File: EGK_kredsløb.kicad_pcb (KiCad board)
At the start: 2 copper layers, 103 x 72 mm, 25 parts, among them U1 INA114AP, U2 MCP6004, U3 MCP6004

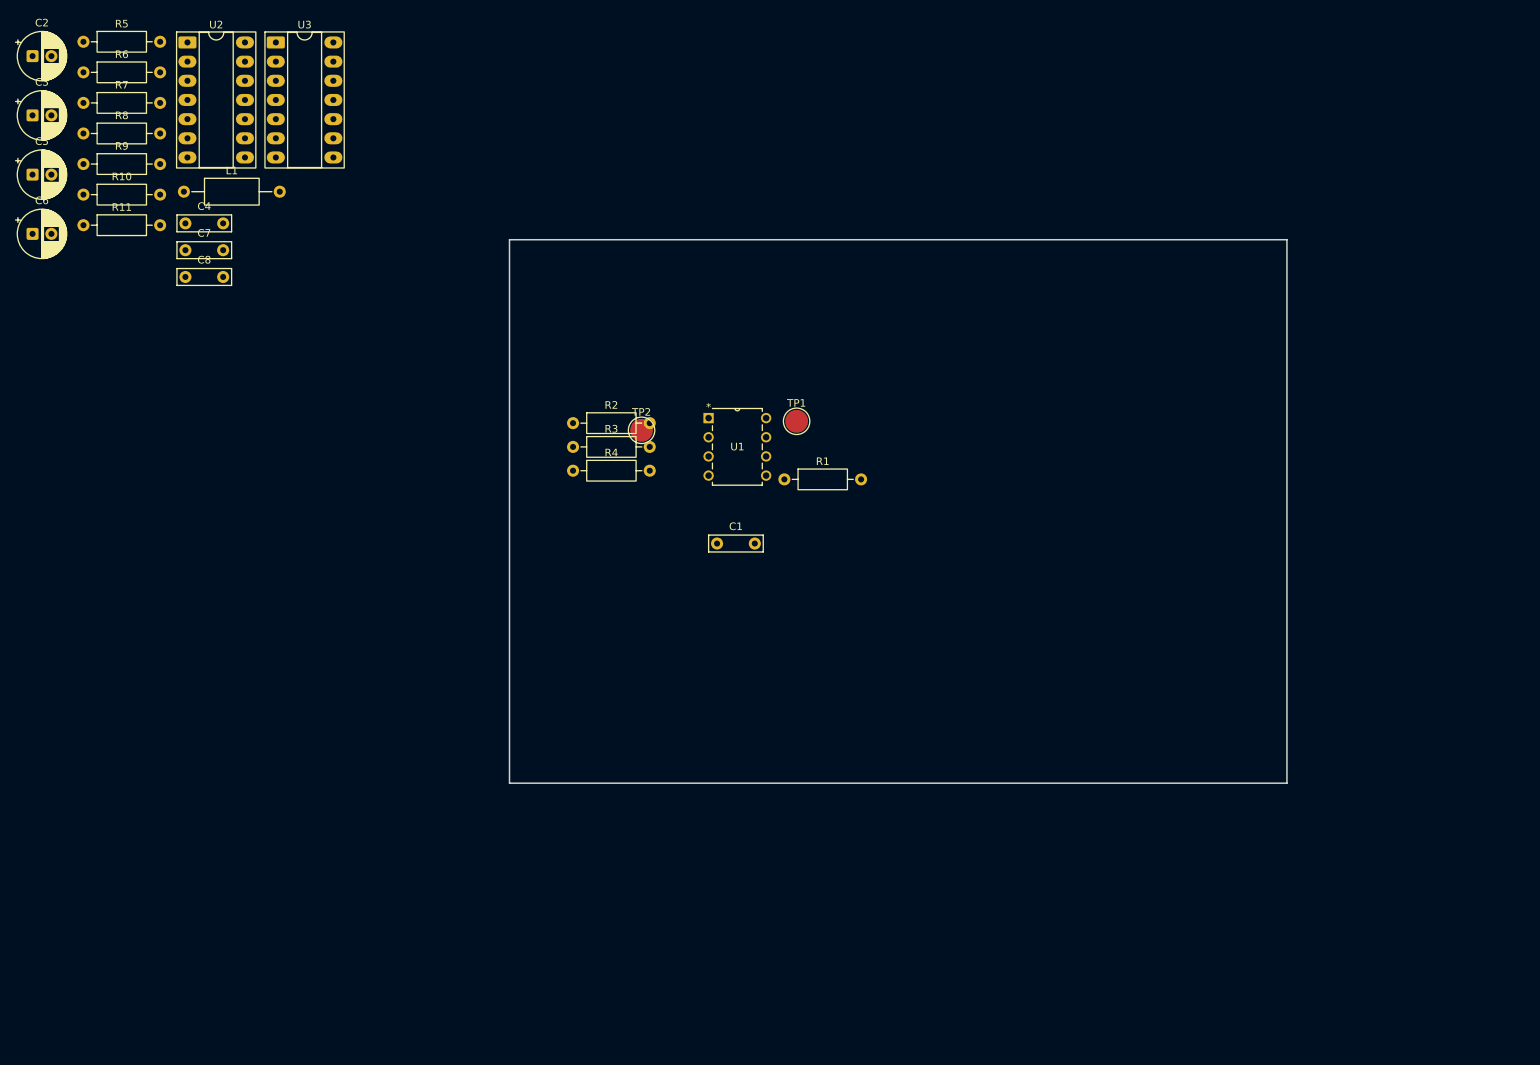
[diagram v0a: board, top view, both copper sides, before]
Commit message: finished schematic, missing AUX
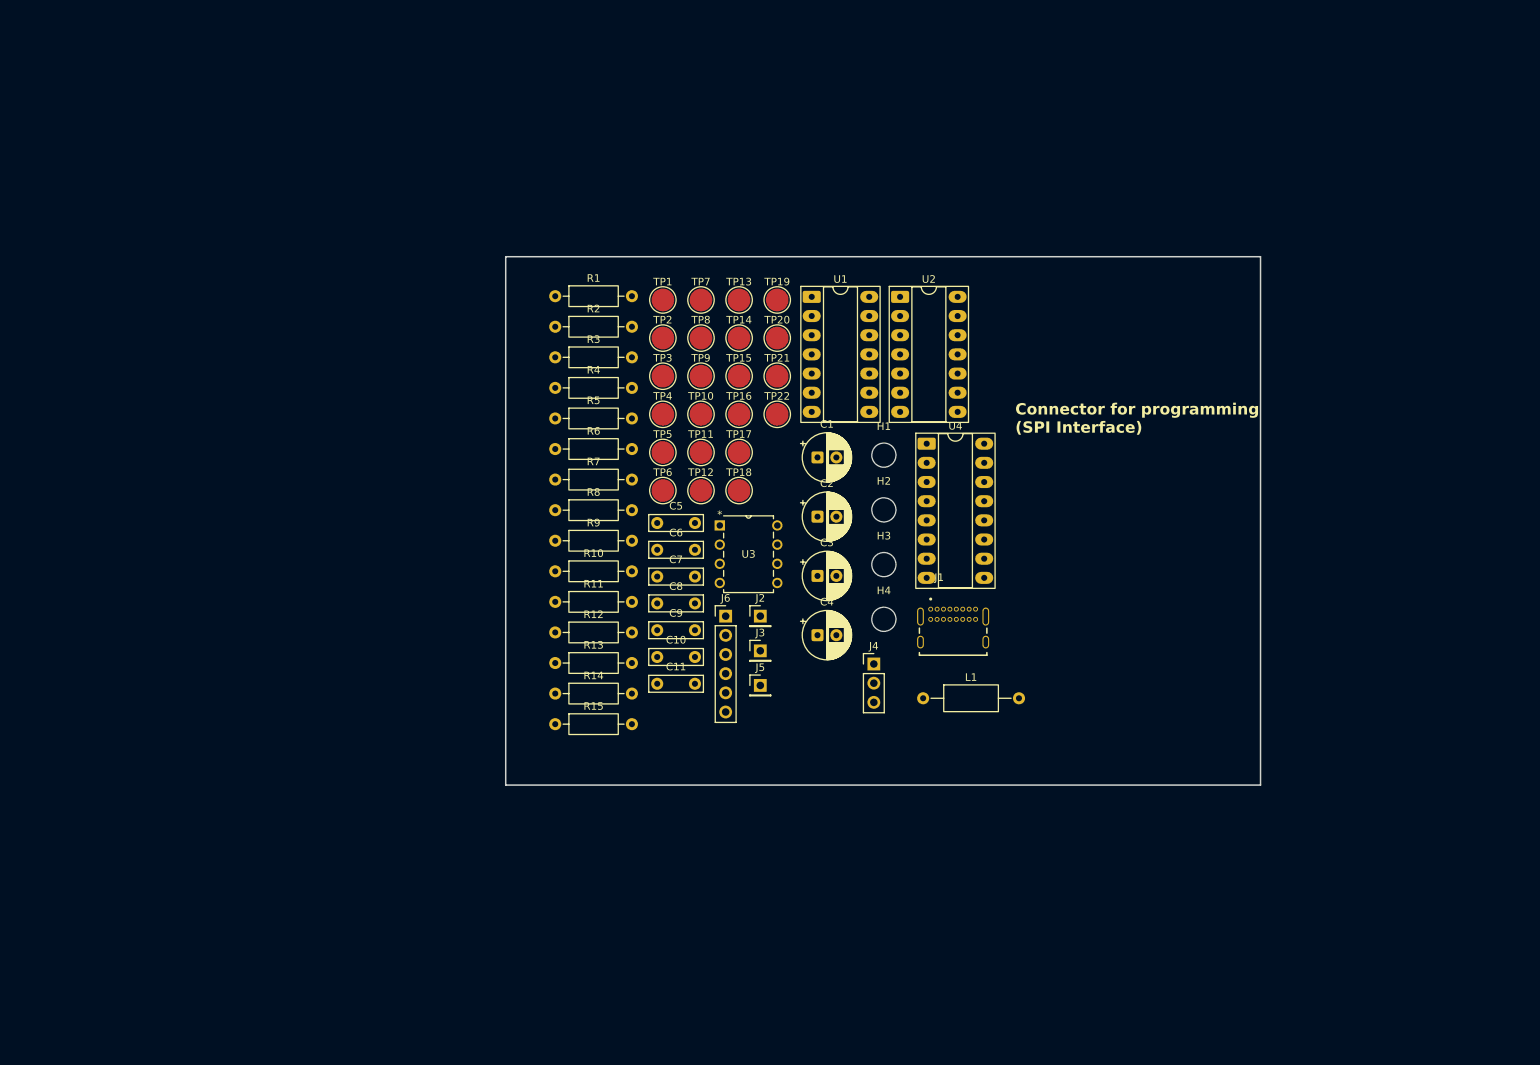
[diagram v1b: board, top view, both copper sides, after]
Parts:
- added C10: 100n, Capacitor_THT:C_Rect_L7.0mm_W2.0mm_P5.00mm, F.Cu at (85.1, 83.0)
- added C11: 10n, Capacitor_THT:C_Rect_L7.0mm_W2.0mm_P5.00mm, F.Cu at (85.1, 86.6)
- added C9: 100n, Capacitor_THT:C_Rect_L7.0mm_W2.0mm_P5.00mm, F.Cu at (85.1, 79.5)
- added H1: MountingHole, MountingHole:MountingHole_3.2mm_M3_ISO7380, F.Cu at (115.1, 56.3)
- added H2: MountingHole, MountingHole:MountingHole_3.2mm_M3_ISO7380, F.Cu at (115.1, 63.5)
- added H3: MountingHole, MountingHole:MountingHole_3.2mm_M3_ISO7380, F.Cu at (115.1, 70.8)
- added H4: MountingHole, MountingHole:MountingHole_3.2mm_M3_ISO7380, F.Cu at (115.1, 78.0)
- added J1: USB4085-GF-A_REVB, connector:GCT_USB4085-GF-A_REVB, F.Cu at (124.3, 81.1)
- added J2: Conn_01x01_Pin, Connector_PinHeader_2.54mm:PinHeader_1x01_P2.54mm_Vertical, F.Cu at (98.7, 77.6)
- added J3: Conn_01x01_Pin, Connector_PinHeader_2.54mm:PinHeader_1x01_P2.54mm_Vertical, F.Cu at (98.7, 82.2)
- added J4: Conn_01x03, Connector_PinHeader_2.54mm:PinHeader_1x03_P2.54mm_Vertical, F.Cu at (113.8, 84.0)
- added J5: Conn_01x01_Pin, Connector_PinHeader_2.54mm:PinHeader_1x01_P2.54mm_Vertical, F.Cu at (98.7, 86.8)
- added J6: Conn_01x06_Pin, Connector_PinHeader_2.54mm:PinHeader_1x06_P2.54mm_Vertical, F.Cu at (94.1, 77.6)
- added R12: 390k, Resistor_THT:R_Axial_DIN0207_L6.3mm_D2.5mm_P10.16mm_Horizontal, F.Cu at (71.6, 79.8)
- added R13: 390k, Resistor_THT:R_Axial_DIN0207_L6.3mm_D2.5mm_P10.16mm_Horizontal, F.Cu at (71.6, 83.8)
- added R14: 10k, Resistor_THT:R_Axial_DIN0207_L6.3mm_D2.5mm_P10.16mm_Horizontal, F.Cu at (71.6, 87.9)
- added R15: 10k, Resistor_THT:R_Axial_DIN0207_L6.3mm_D2.5mm_P10.16mm_Horizontal, F.Cu at (71.6, 91.9)
- added TP10: TestPoint, TestPoint:TestPoint_Pad_D3.0mm, F.Cu at (90.9, 50.9)
- added TP11: TestPoint, TestPoint:TestPoint_Pad_D3.0mm, F.Cu at (90.9, 55.9)
- added TP12: TestPoint, TestPoint:TestPoint_Pad_D3.0mm, F.Cu at (90.9, 61.0)
- added TP13: TestPoint, TestPoint:TestPoint_Pad_D3.0mm, F.Cu at (95.9, 35.7)
- added TP14: TestPoint, TestPoint:TestPoint_Pad_D3.0mm, F.Cu at (95.9, 40.8)
- added TP15: TestPoint, TestPoint:TestPoint_Pad_D3.0mm, F.Cu at (95.9, 45.8)
- added TP16: TestPoint, TestPoint:TestPoint_Pad_D3.0mm, F.Cu at (95.9, 50.9)
- added TP17: TestPoint, TestPoint:TestPoint_Pad_D3.0mm, F.Cu at (95.9, 55.9)
- added TP18: TestPoint, TestPoint:TestPoint_Pad_D3.0mm, F.Cu at (95.9, 61.0)
- added TP19: TestPoint, TestPoint:TestPoint_Pad_D3.0mm, F.Cu at (101.0, 35.7)
- added TP20: TestPoint, TestPoint:TestPoint_Pad_D3.0mm, F.Cu at (101.0, 40.8)
- added TP21: TestPoint, TestPoint:TestPoint_Pad_D3.0mm, F.Cu at (101.0, 45.8)
- added TP22: TestPoint, TestPoint:TestPoint_Pad_D3.0mm, F.Cu at (101.0, 50.9)
- added TP3: TestPoint, TestPoint:TestPoint_Pad_D3.0mm, F.Cu at (85.8, 45.8)
- added TP4: TestPoint, TestPoint:TestPoint_Pad_D3.0mm, F.Cu at (85.8, 50.9)
- added TP5: TestPoint, TestPoint:TestPoint_Pad_D3.0mm, F.Cu at (85.8, 55.9)
- added TP6: TestPoint, TestPoint:TestPoint_Pad_D3.0mm, F.Cu at (85.8, 61.0)
- added TP7: TestPoint, TestPoint:TestPoint_Pad_D3.0mm, F.Cu at (90.9, 35.7)
- added TP8: TestPoint, TestPoint:TestPoint_Pad_D3.0mm, F.Cu at (90.9, 40.8)
- added TP9: TestPoint, TestPoint:TestPoint_Pad_D3.0mm, F.Cu at (90.9, 45.8)
- added U4: MCP3208, Package_DIP:DIP-16_W7.62mm_Socket_LongPads, F.Cu at (120.8, 54.8)
- C1: value 100n -> 10μ; footprint Capacitor_THT:C_Rect_L7.0mm_W2.0mm_P5.00mm -> Capacitor_THT:CP_Radial_D6.3mm_P2.50mm
- C3: value 1μ -> 10μ
- C4: value 100n -> 1μ; footprint Capacitor_THT:C_Rect_L7.0mm_W2.0mm_P5.00mm -> Capacitor_THT:CP_Radial_D6.3mm_P2.50mm
- C5, C6: value 10μ -> 100n; footprint Capacitor_THT:CP_Radial_D6.3mm_P2.50mm -> Capacitor_THT:C_Rect_L7.0mm_W2.0mm_P5.00mm
- C7: value 300n -> 150n
- C8: value 150n -> 300n
- R1: value 100k -> 20
- R10: value 7.5k -> 100k
- R11: value 7.5k -> 51
- R2: value 51 -> 470k
- R3: value 51 -> 240k
- R4: value 100k -> 15k
- R5: value 20 -> 15k
- R6, R7: value 15k -> 7.5k
- R8: value 240k -> 10k
- R9: value 470k -> 100k
- U1: value INA114AP -> MCP6004; footprint packages:PDIP8 -> Package_DIP:DIP-14_W7.62mm_Socket_LongPads
- U3: value MCP6004 -> INA114AP; footprint Package_DIP:DIP-14_W7.62mm_Socket_LongPads -> packages:PDIP8
- moved C2 120.6 mm to (106.3, 64.4)
- moved C3 120.6 mm to (106.3, 72.3)
- moved L1 118.7 mm to (120.3, 88.5)
- moved U2 100.3 mm to (117.2, 35.3)
- moved C4 99.9 mm to (106.3, 80.1)
- moved U3 97.7 mm to (101.0, 73.2)
- moved C5 94.8 mm to (85.1, 65.3)
- moved C6 92.7 mm to (85.1, 68.8)
- moved R10 80.0 mm to (71.6, 71.7)
- moved R11 80.0 mm to (71.6, 75.7)
- moved R5 80.0 mm to (71.6, 51.4)
- moved R6 80.0 mm to (71.6, 55.5)
- moved R7 80.0 mm to (71.6, 59.5)
- moved R8 80.0 mm to (71.6, 63.6)
- moved R9 80.0 mm to (71.6, 67.6)
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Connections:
- C1 pad 1: +5V -> Net-(C1-Pad1)
- C1 pad 2: GND -> /SIGNAL_AMP
- C2 pad 1: +5V -> Net-(U1B-+)
- C2 pad 2: Net-(C2-Pad2) -> Net-(C1-Pad1)
- C3 pad 1: Net-(U2A-+) -> +5V
- C3 pad 2: GND -> Net-(C3-Pad2)
- C4 pad 1: +5V -> /V_BIAS
- C5 pad 1: Net-(C5-Pad1) -> +5V
- C5 pad 2: /SIGNAL_INA -> GND
- C6 pad 1: Net-(U3A-+) -> +5V
- C6 pad 2: Net-(C5-Pad1) -> GND
- C7 pad 1: Net-(C7-Pad1) -> /VGND
- C7 pad 2: /SIGNAL_OUT -> Net-(U2C-+)
- C8 pad 1: /VGND -> Net-(C8-Pad1)
- C8 pad 2: Net-(U3B-+) -> /SIGNAL_OUT
- L1 pad 1: +5V -> /5V_USB
- L1 pad 2: GND -> +5V
- R1 pad 1: /L_ARM -> GND
- R1 pad 2: /V+IN -> Net-(C3-Pad2)
- R10 pad 1: Net-(C7-Pad1) -> /R_ARM
- R10 pad 2: /SIGNAL_HP -> /V-IN
- R11 pad 1: Net-(U3B-+) -> /RightLegDrive
- R11 pad 2: Net-(C7-Pad1) -> /RG2
- R2 pad 1: /RightLegDrive -> /VGND
- R2 pad 2: /RG1 -> Net-(U1B-+)
- R3 pad 1: /RightLegDrive -> /SIGNAL_HP
- R3 pad 2: /RG2 -> Net-(C1-Pad1)
- R4 pad 1: /R_ARM -> /V_BIAS
- R4 pad 2: /V-IN -> +5V
- R5 pad 2: Net-(C2-Pad2) -> /V_BIAS
- R6 pad 1: Net-(U2A-+) -> Net-(C8-Pad1)
- R6 pad 2: +5V -> /SIGNAL_HP
- R7 pad 1: GND -> Net-(U2C-+)
- R7 pad 2: Net-(U2A-+) -> Net-(C8-Pad1)
- R8 pad 1: /SIGNAL_HP -> Net-(U1C--)
- R8 pad 2: Net-(C5-Pad1) -> Net-(U2B--)
- R9 pad 1: /VGND -> /L_ARM
- R9 pad 2: Net-(U3A-+) -> /V+IN
- TP1 pad 1: /V+IN -> /SIGNAL_AMP
- TP2 pad 1: /V-IN -> /VGND
- U1 pad 1: /RG1 -> /VGND
- U1 pad 2: /V-IN -> /VGND
- U1 pad 3: /V+IN -> /V_BIAS
- U1 pad 4: GND -> +5V
- U1 pad 5: /VGND -> Net-(U1B-+)
- U1 pad 6: /INA_OUT -> /SIGNAL_HP
- U1 pad 7: +5V -> /SIGNAL_HP
- U1 pad 8: /RG2 -> Net-(R12-Pad1)
- U2 pad 1: /VGND -> /SIGNAL_AMP
- U2 pad 10: (no net) -> Net-(U2C-+)
- U2 pad 12: (no net) -> unconnected-(U2D-+-Pad12)
- U2 pad 13: (no net) -> unconnected-(U2D---Pad13)
- U2 pad 14: (no net) -> unconnected-(U2-Pad14)
- U2 pad 2: /VGND -> Net-(U2A--)
- U2 pad 3: Net-(U2A-+) -> /INA_OUT
- U2 pad 5: (no net) -> /RightLegDrive
- U2 pad 6: (no net) -> Net-(U2B--)
- U2 pad 7: (no net) -> Net-(U2B--)
- U2 pad 8: (no net) -> /SIGNAL_OUT
- U2 pad 9: (no net) -> /SIGNAL_OUT
- U3 pad 1: /SIGNAL_HP -> /RightLegDrive
- U3 pad 2: /SIGNAL_HP -> /V-IN
- U3 pad 3: Net-(U3A-+) -> /V+IN
- U3 pad 4: (no net) -> GND
- U3 pad 5: Net-(U3B-+) -> /VGND
- U3 pad 6: /SIGNAL_OUT -> /INA_OUT
- U3 pad 7: /SIGNAL_OUT -> +5V
- U3 pad 8: (no net) -> /RG2
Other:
- board size 103 x 72 mm -> 100 x 70 mm
- board text added: "Connector for programming (SPI Interface)"

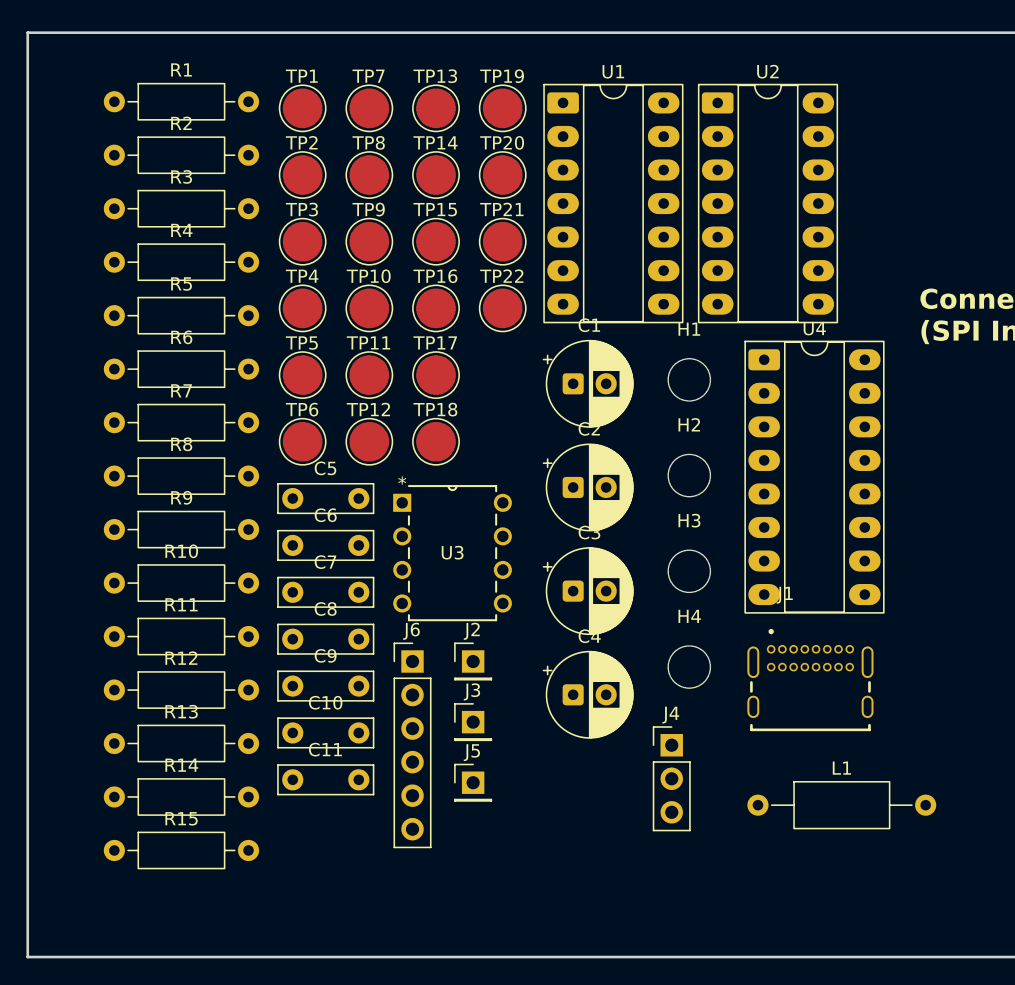
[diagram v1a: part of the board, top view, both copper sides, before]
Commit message: opdateret med micro-usb samt 3.5mm audio jack til elektroder
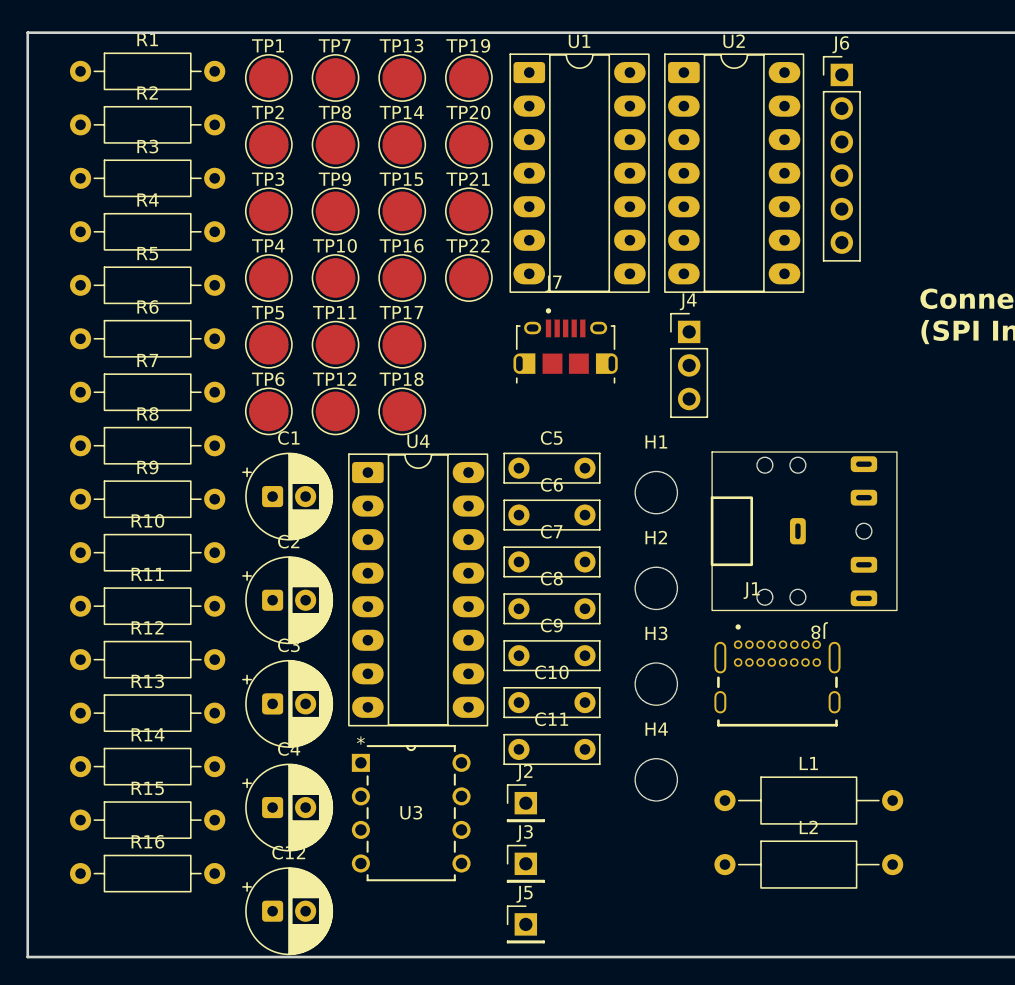
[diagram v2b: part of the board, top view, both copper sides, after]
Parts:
- added C12: 10μ, Capacitor_THT:CP_Radial_D6.3mm_P2.50mm, F.Cu at (83.5, 96.5)
- added J7: 10118194-0001LF, connector:AMPHENOL_10118194-0001LF, F.Cu at (105.7, 55.1)
- added J8: Mini_Jack_5pins, mini_jack_5pins.kicad_mod:mini_jack_5pins, F.Cu at (128.3, 67.8)
- added L2: 1m, Inductor_THT:L_Axial_L7.0mm_D3.3mm_P12.70mm_Horizontal_Fastron_MICC, F.Cu at (117.8, 93.0)
- added R16: 20, Resistor_THT:R_Axial_DIN0207_L6.3mm_D2.5mm_P10.16mm_Horizontal, F.Cu at (69.0, 93.7)
- moved J6 55.0 mm to (126.7, 33.2)
- moved J4 31.3 mm to (115.1, 52.7)
- moved U4 31.2 mm to (90.8, 63.3)
- moved C2 24.3 mm to (83.5, 73.0)
- moved C4 24.3 mm to (83.5, 88.7)
- moved C1 24.3 mm to (83.5, 65.1)
- moved C3 24.3 mm to (83.5, 80.8)
- moved U3 19.9 mm to (97.9, 92.9)
- moved C10 17.3 mm to (102.2, 80.7)
- moved C11 17.3 mm to (102.2, 84.3)
- moved C5 17.3 mm to (102.2, 63.0)
- moved C6 17.3 mm to (102.2, 66.5)
- moved C7 17.3 mm to (102.2, 70.1)
- moved C8 17.3 mm to (102.2, 73.6)
- moved C9 17.3 mm to (102.2, 77.2)
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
